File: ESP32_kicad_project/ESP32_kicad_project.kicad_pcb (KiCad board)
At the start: 2 copper layers, 30 x 60 mm, 68 parts, among them J1 Conn_01x04_Pin, J2 USB_C_Receptacle_USB2.0_16P, Q1 AO3401A, Q2 SS8050, Q3 SS8050, SW1 SW_Push, SW2 SW_Push, U1 TPS56339DDC, U2 ESP32-WROOM-32E, U3 CP2102N-Axx-xQFN24

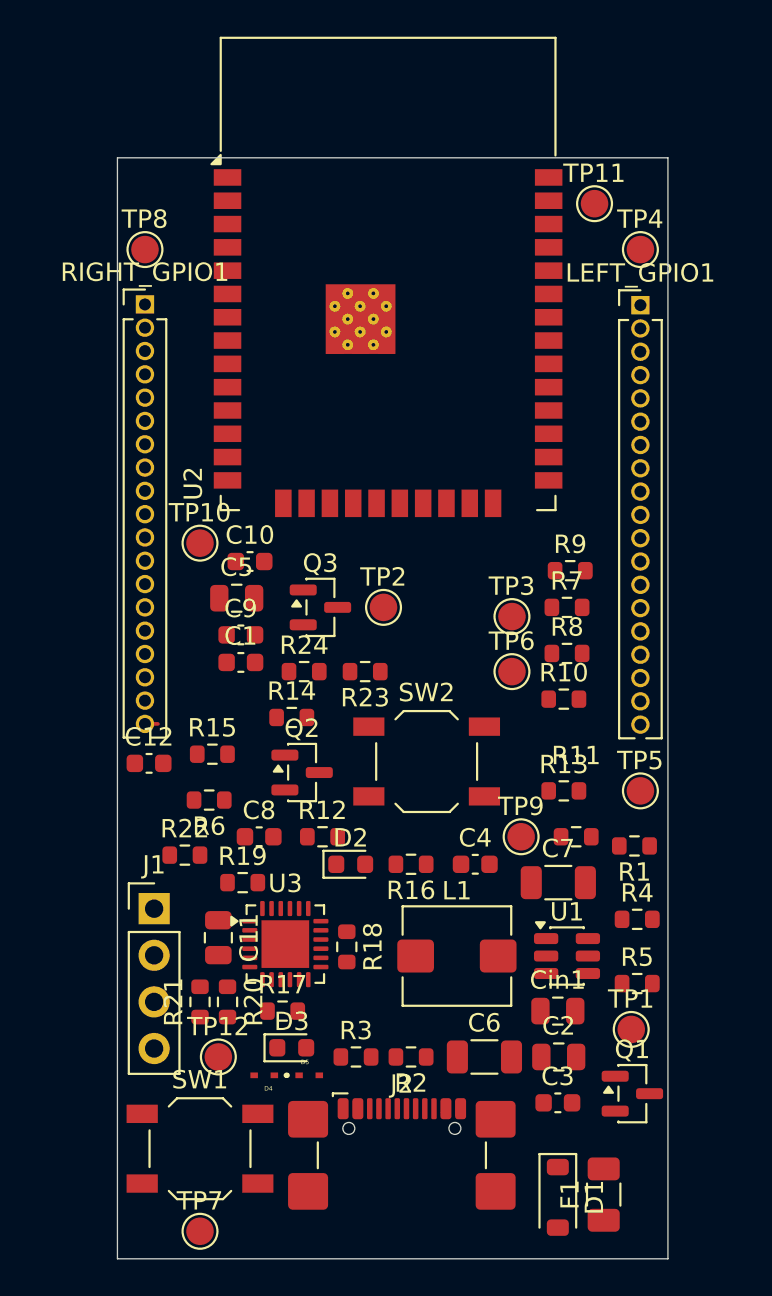
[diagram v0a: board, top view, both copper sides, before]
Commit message: routed the regulator properly, VBUS and 3V3 are also routed
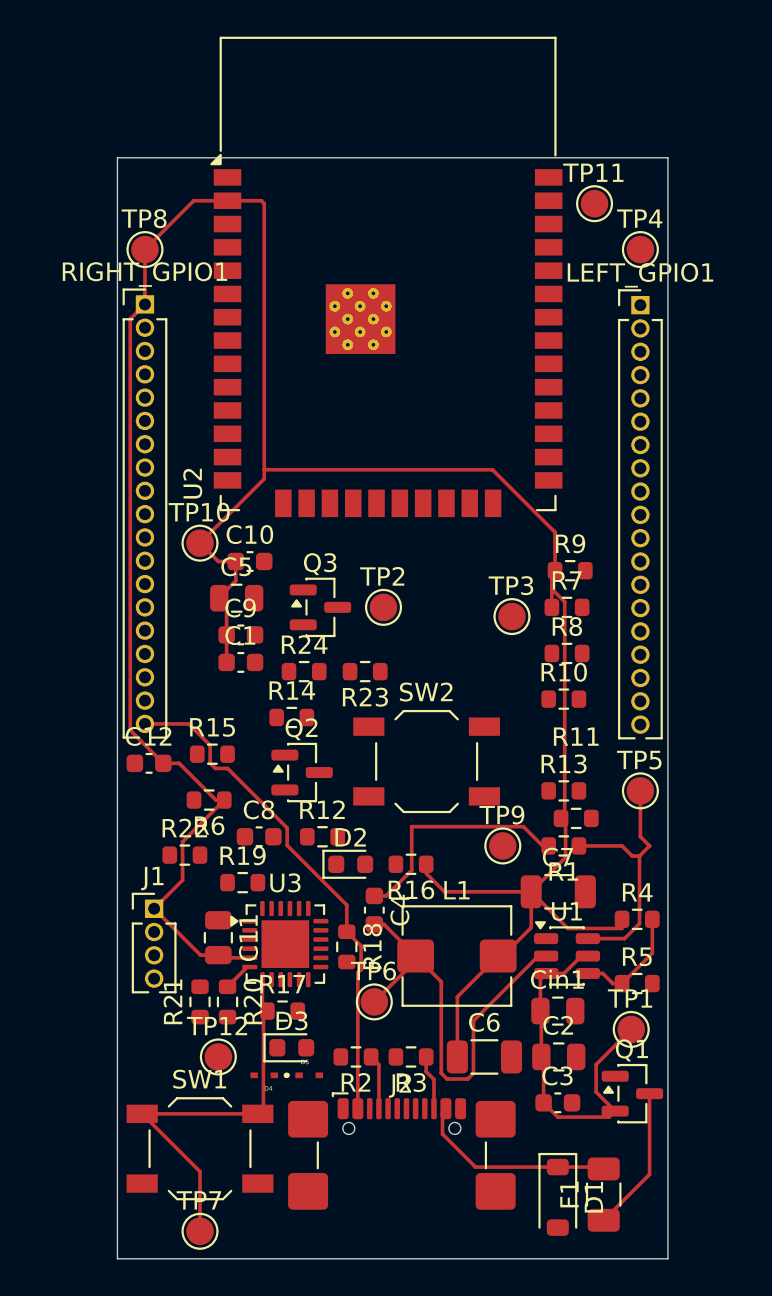
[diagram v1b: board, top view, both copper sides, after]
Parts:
- J1: footprint Connector_PinHeader_2.54mm:PinHeader_1x04_P2.54mm_Vertical -> Connector_PinHeader_1.27mm:PinHeader_1x04_P1.27mm_Vertical
- moved TP6 19.5 mm to (217.0, 107.5)
- moved C4 6.04 mm to (217.0, 102.5), turned to -90 degrees
- moved R1 3.85 mm to (227.3, 99.0)
- moved R2 3.00 mm to (216.0, 110.5)
- moved R3 3.00 mm to (219.0, 110.5), turned to 180 degrees
- moved TP9 1.12 mm to (224.0, 99.0)
- moved R11 1.00 mm to (228.0, 97.5)
- moved C7 0.50 mm to (227.0, 101.5)
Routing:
- net /ESP32 Core/3V3: track 0.00 -> 168.6 mm
- net /ESP32 Core/VBUS: track 1.11 -> 38.7 mm
- net Net-(U1-SW): track 0.00 -> 23.7 mm
- net Net-(Q1-S): track 0.00 -> 19.9 mm
- net Net-(U1-BOOT): track 0.00 -> 14.7 mm
- net Net-(C4-Pad1): track 0.00 -> 12.6 mm
- net Net-(Q1-D): track 0.00 -> 7.94 mm
- net Net-(U1-FB): track 0.00 -> 6.27 mm
- net Net-(J2-CC2): track 0.00 -> 3.00 mm
- net Net-(J2-CC1): track 0.00 -> 3.00 mm

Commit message: done routing, needs GND routing now
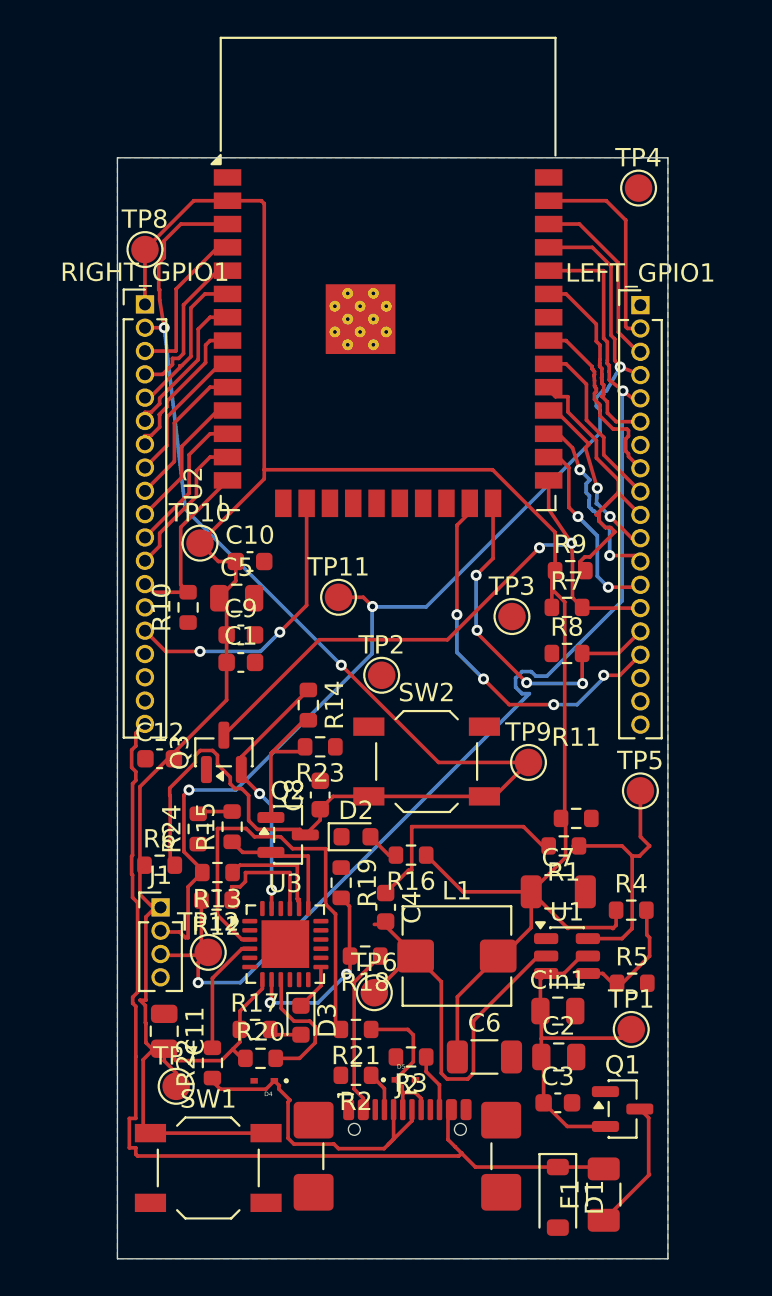
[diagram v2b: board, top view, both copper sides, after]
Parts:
- moved TP11 25.6 mm to (215.1, 85.5)
- moved R10 21.1 mm to (206.8, 86.0), turned to 90 degrees
- moved R13 19.4 mm to (208.4, 100.5), turned to 180 degrees
- moved R22 11.4 mm to (208.2, 110.8), turned to 90 degrees
- moved R24 10.3 mm to (207.4, 98.1), turned to 90 degrees
- moved Q3 9.49 mm to (208.8, 93.9), turned to 90 degrees
- moved R21 8.63 mm to (216.0, 109.0), turned to 180 degrees
- moved TP7 8.01 mm to (206.2, 112.1)
- moved R12 6.73 mm to (208.4, 102.0), turned to 180 degrees
- moved C11 5.89 mm to (205.6, 109.1)
- moved TP12 5.73 mm to (207.9, 104.8)
- moved R19 5.37 mm to (215.2, 101.0), turned to -90 degrees
- moved D5 5.25 mm to (218.7, 111.7)
- moved R23 4.78 mm to (214.1, 93.6)
- moved TP9 4.76 mm to (225.4, 94.5)
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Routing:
- net /ESP32 Core/EN_IN: track 0.00 -> 74.3 mm, vias 0 -> 2
- net /ESP32 Core/RX0: track 0.00 -> 64.0 mm, vias 0 -> 2
- net /ESP32 Core/TX0: track 0.00 -> 59.5 mm, vias 0 -> 3
- net /ESP32 Core/IO0: track 0.00 -> 34.0 mm, vias 0 -> 2
- net /ESP32 Core/VBUS: track 38.7 -> 62.8 mm
- net Net-(U3-D+): track 0.00 -> 23.6 mm
- net /ESP32 Core/IO15: track 0.00 -> 20.8 mm, vias 0 -> 4
- net /ESP32 Core/IO2: track 0.00 -> 19.7 mm, vias 0 -> 4
- net /ESP32 Core/IO5: track 0.00 -> 17.8 mm
- net /Power/USB_D-: track 0.00 -> 17.5 mm
- net /ESP32 Core/3V3: track 168.6 -> 152.5 mm
- net /ESP32 Core/IO13: track 0.00 -> 15.9 mm, vias 0 -> 2
- net /USB-UART/DTR: track 0.00 -> 14.1 mm, vias 0 -> 2
- net /ESP32 Core/IO23: track 0.00 -> 11.3 mm
- net /ESP32 Core/IO4: track 0.00 -> 10.6 mm, vias 0 -> 2
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- added copper zone on B.Cu, net GND

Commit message: routed GND, next step is : correct DRC errors
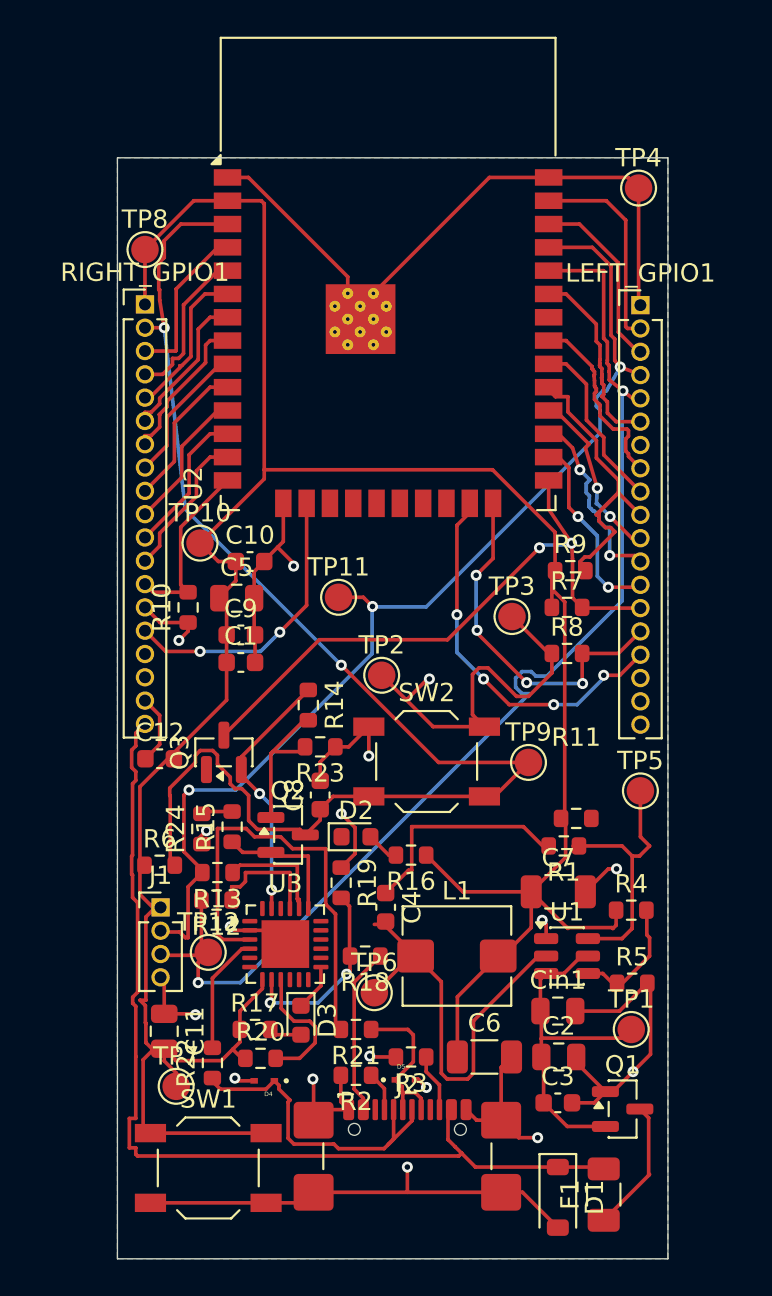
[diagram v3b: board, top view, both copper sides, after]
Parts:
- moved R24 0.20 mm to (207.6, 98.1)
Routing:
- net GND: track 0.00 -> 162.6 mm, vias 0 -> 17
- net Net-(U3-D+): track 23.6 -> 24.2 mm

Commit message: added media
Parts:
- moved TP6 7.83 mm to (221.8, 100.8)
- moved U1 2.29 mm to (229.8, 104.5)
- moved C3 1.60 mm to (227.1, 111.4)
- moved C2 1.17 mm to (227.8, 109.6)
- moved R4 1.10 mm to (231.1, 101.4)
- moved Cin1 0.92 mm to (226.8, 107.1)
- moved D1 0.91 mm to (227.9, 118.0)
- moved F1 0.90 mm to (230.4, 118.0)
- moved R19 0.83 mm to (215.9, 101.3)
- moved R18 0.75 mm to (217.2, 105.0), turned to 90 degrees
- moved C4 0.62 mm to (217.4, 101.8)
- moved R5 0.52 mm to (231.1, 107.0)
- moved TP4 0.25 mm to (231.2, 63.3)
- moved J1 0.20 mm to (205.2, 102.3)
- moved J2 0.10 mm to (218.9, 117.0)
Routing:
- net GND: track 162.6 -> 189.3 mm
- net /ESP32 Core/IO15: track 20.8 -> 30.8 mm
- net Net-(D2-K): track 0.00 -> 8.30 mm, vias 0 -> 2
- net Net-(Q1-S): track 18.9 -> 24.5 mm
- net /ESP32 Core/VBUS: track 62.8 -> 66.8 mm, vias 0 -> 2
- net Net-(U1-SW): track 23.4 -> 19.7 mm
- net Net-(Q3-B): track 1.70 -> 4.22 mm
- net Net-(U1-BOOT): track 14.4 -> 12.0 mm
- net Net-(U3-D+): track 24.2 -> 26.5 mm
- net Net-(U3-VBUS): track 10.5 -> 12.8 mm
- net Net-(U1-FB): track 6.77 -> 8.50 mm
- net /Power/USB_D-: track 17.5 -> 16.4 mm
- net /ESP32 Core/3V3: track 152.5 -> 152.8 mm, vias 0 -> 2
